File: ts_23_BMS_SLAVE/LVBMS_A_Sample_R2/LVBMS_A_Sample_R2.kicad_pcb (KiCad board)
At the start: 2 copper layers, 48.2 x 53.5 mm, 132 parts, among them J1 S2B-PH-K-S_LF__SN_, J2 Conn_01x13_Male, J3 S2B-PH-K-S_LF__SN_, J4 Conn_02x05_Counter_Clockwise, Q1 BSS308PE_H6327, Q10 BSS308PE_H6327, Q11 BSS308PE_H6327, Q12 BSS308PE_H6327, Q13 BSS308PE_H6327, Q14 BSS308PE_H6327, Q15 DTC114E, Q2 CZT5551CT-ND, Q3 BSS308PE_H6327, Q4 BSS308PE_H6327, Q5 BSS308PE_H6327, Q6 BSS308PE_H6327, Q7 BSS308PE_H6327, Q8 BSS308PE_H6327, Q9 BSS308PE_H6327, T1 HX1188NL, U1 LTC6811

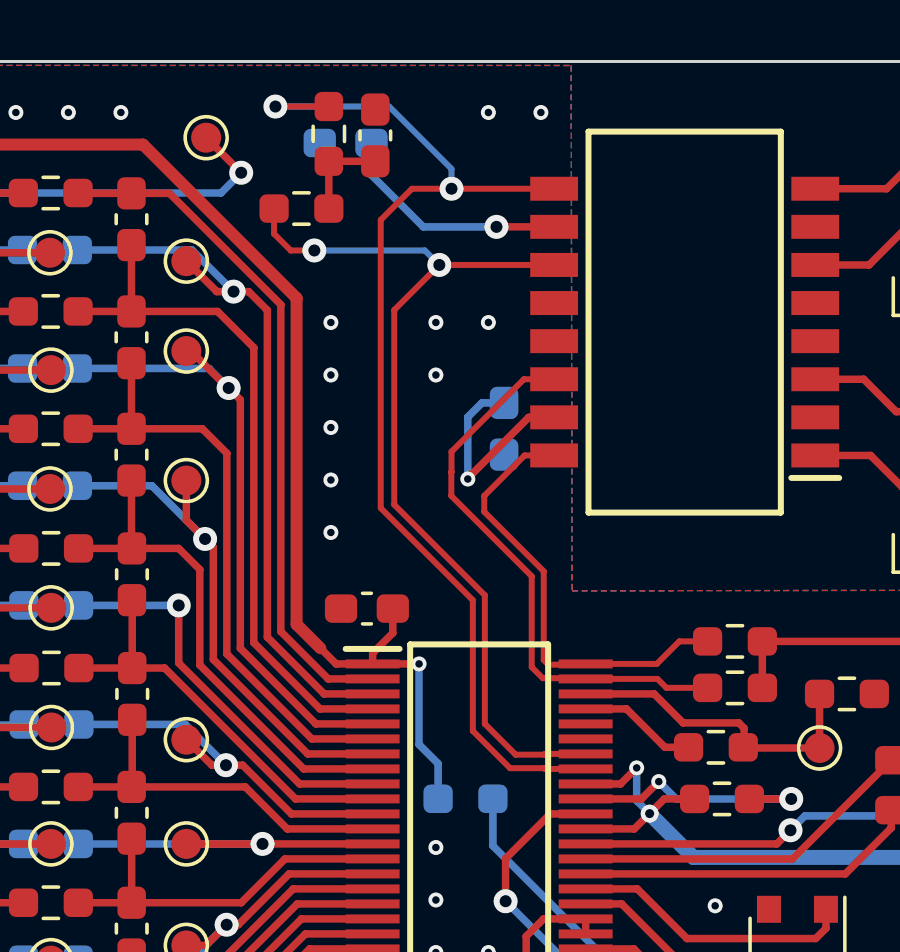
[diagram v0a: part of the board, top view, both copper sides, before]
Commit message: Fix Diff. Pair Routing on Slave
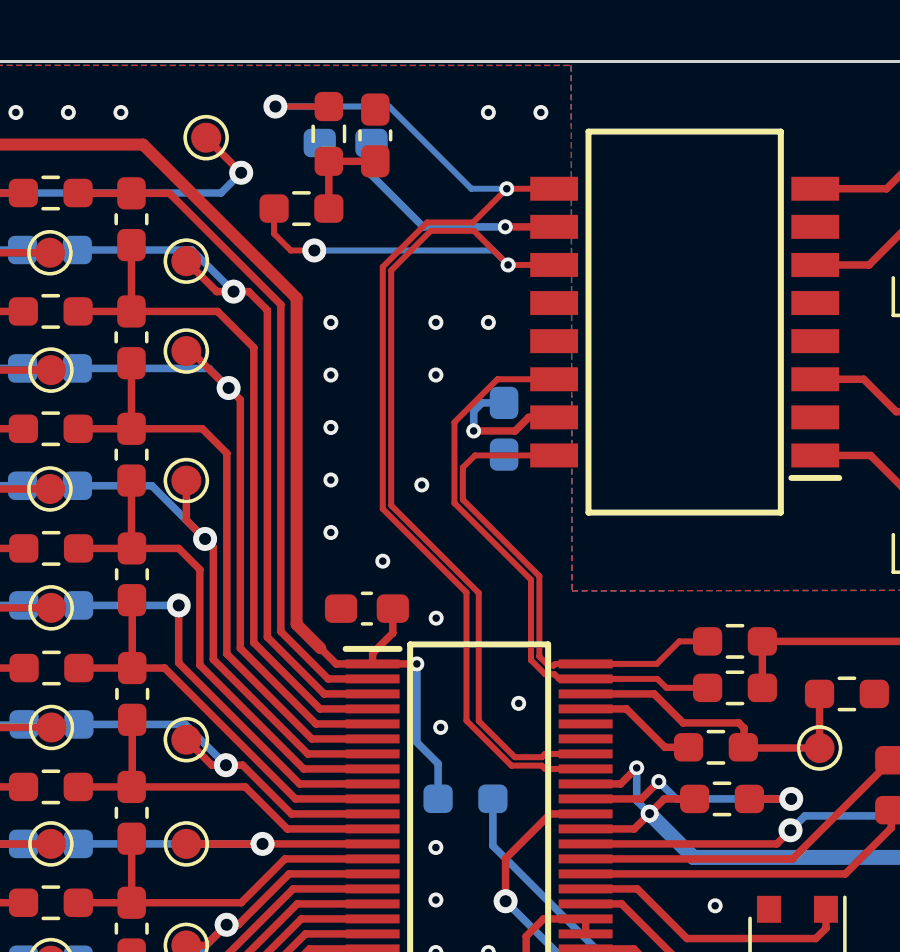
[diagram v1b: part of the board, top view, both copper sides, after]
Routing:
- net /ISO_SPI_P: track 31.6 -> 35.9 mm
- net Net-(C1-Pad2): track 7.21 -> 4.66 mm
- net /ISO_SPI_+: track 15.0 -> 16.6 mm
- net GND: vias 136 -> 141

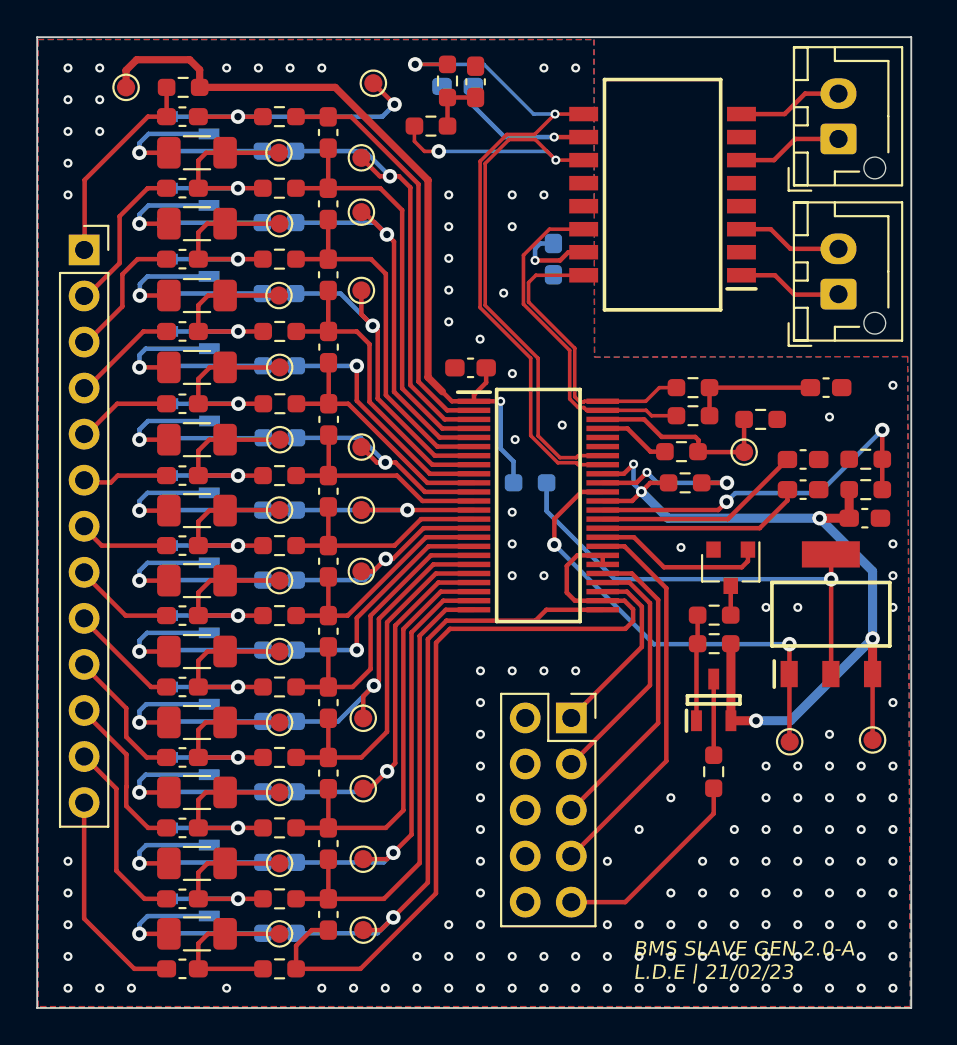
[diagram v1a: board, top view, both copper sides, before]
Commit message: LV BMS Updates
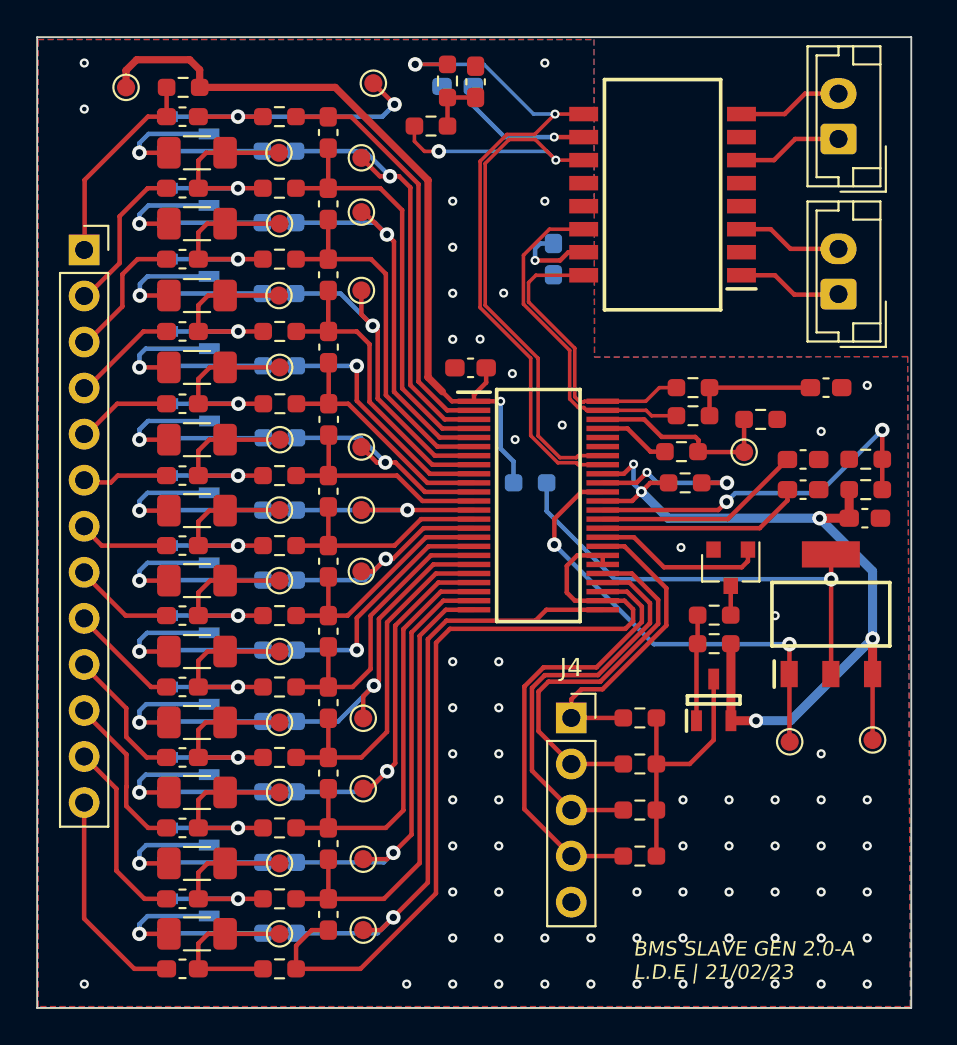
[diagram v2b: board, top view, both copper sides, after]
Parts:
- added R50: 100k, Resistor_SMD:R_0603_1608Metric_Pad0.98x0.95mm_HandSolder, F.Cu at (158.4, 105.2)
- added R51: 100k, Resistor_SMD:R_0603_1608Metric_Pad0.98x0.95mm_HandSolder, F.Cu at (158.4, 107.7)
- added R54: 100k, Resistor_SMD:R_0603_1608Metric_Pad0.98x0.95mm_HandSolder, F.Cu at (158.4, 110.2)
- J1, J3: footprint Connector_JST:JST_XH_B2B-XH-AM_1x02_P2.50mm_Vertical -> Connector_JST:JST_EH_B2B-EH-A_1x02_P2.50mm_Vertical
- J4: value Conn_02x05_Counter_Clockwise -> Conn_01x05_Male; footprint Connector_PinSocket_2.54mm:PinSocket_2x05_P2.54mm_Vertical -> Connector_PinSocket_2.54mm:PinSocket_1x05_P2.54mm_Vertical
- moved R2 5.04 mm to (158.4, 102.6), turned to 0 degrees
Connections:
- J4 pad 2: GND -> /T2
- J4 pad 3: /T2 -> /T3
- J4 pad 4: GND -> /T4
- J4 pad 5: /T3 -> GND
- R2 pad 1: Net-(J4-Pad9) -> /T1
- U1 pad 27: /T1 -> /T4
- U1 pad 28: /T2 -> /T3
- U1 pad 29: /T3 -> /T2
- U1 pad 32: /T4 -> /T1
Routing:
- net Net-(J4-Pad9): track 11.3 -> 0.00 mm
- net /VTEMP: track 4.20 -> 14.7 mm
- net /T1: track 10.3 -> 17.3 mm
- net /T2: track 13.7 -> 20.7 mm
- net /T3: track 17.2 -> 22.7 mm
- net /T4: track 21.4 -> 24.6 mm
- net GND: vias 141 -> 68
